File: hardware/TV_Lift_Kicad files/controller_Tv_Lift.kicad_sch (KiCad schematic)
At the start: 102 parts, among them J1 socket LAN8720a, J10 1844210, J11 1844223, J12 C5360899, J2 1836189, J3 1844223, J4 1844210, J5 1844223, J6 1844223, J7 1844236, J8 C5360899, J9 1844210, Q2 MMBT3906, SW1 TS-1187A-BAB, SW2 TS-1187A-BAB, SW3 TS-1187A-BAB, SW4 TS-1187A-BAB, U1 MAX3232, U10 VNH5019A-E, U2 TSOP32S40F, U3 SN65HVD230, U4 ESP32-WROOM-32, U5 LM2596S-5, U6 AMS1117-3.3, U7 PC817, U8 PC817, U9 b0505s-1we

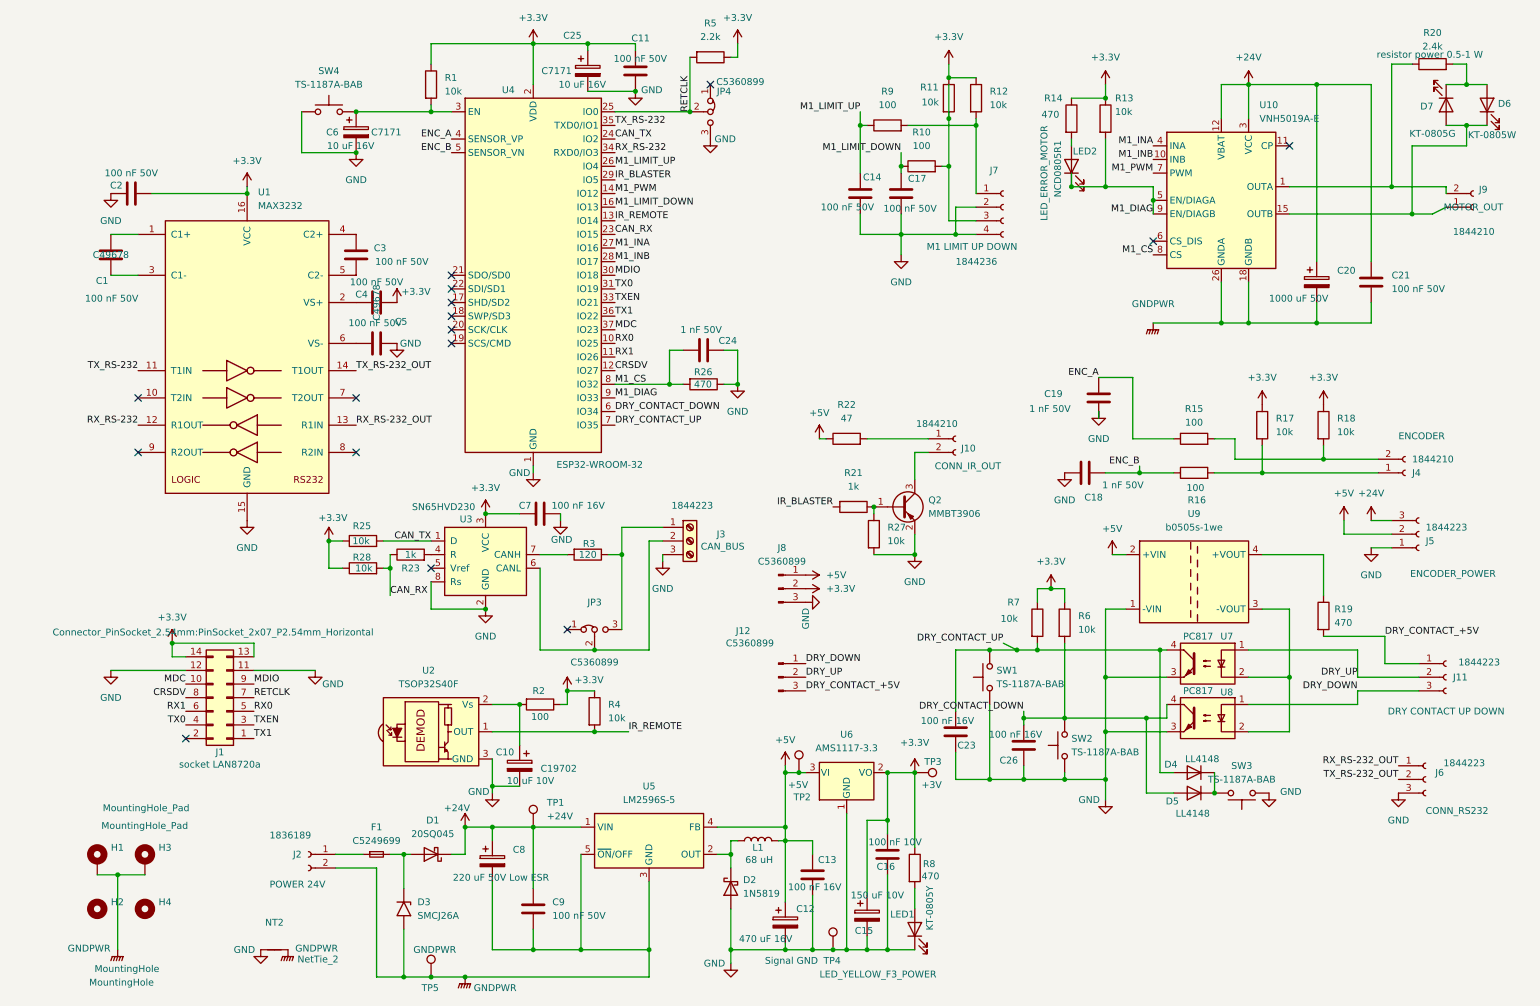
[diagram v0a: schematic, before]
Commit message: finish pcb board change pins
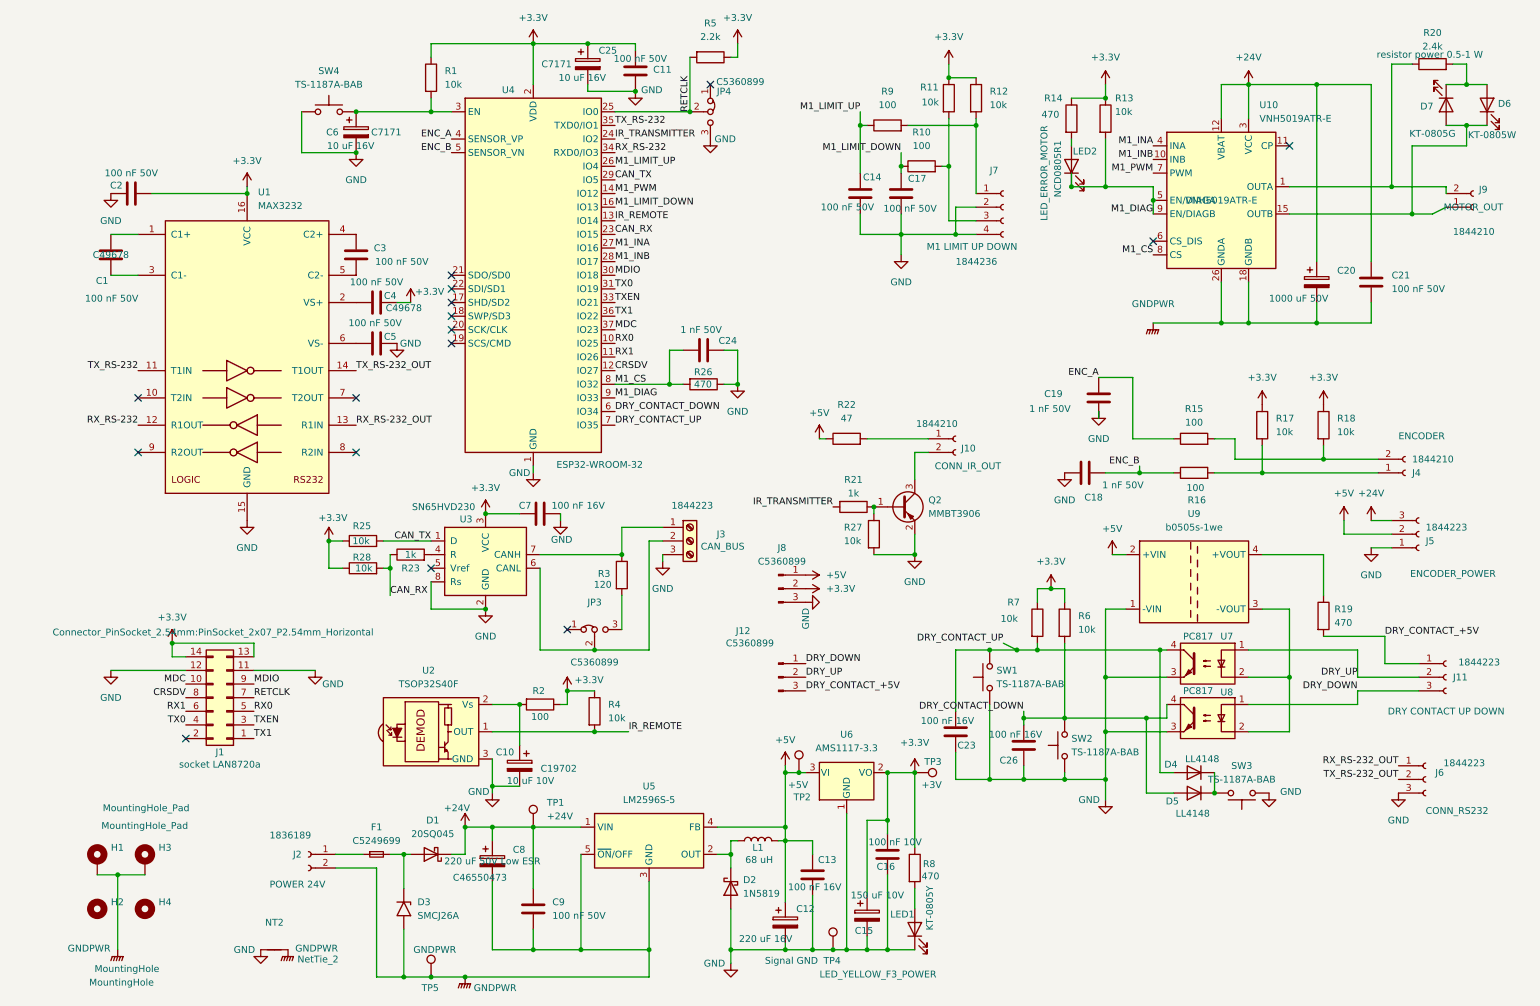
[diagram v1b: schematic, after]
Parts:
- C12: value 470 uF 16V -> 220 uF 16V
- C8: value 220 uF 50V Low ESR -> C46550473; footprint Capacitor_THT:CP_Radial_D6.3mm_P2.50mm -> Capacitor_SMD:CP_Elec_10x10
- TP1, TP2, TP3, TP4, TP5: now left out of the parts list
- U10: value VNH5019A-E -> VNH5019ATR-E
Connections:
- net CAN_TX: now also U4.29 (IO5); no longer U4.24 (IO2)
- net at J3.1 (Pin_1), R3.1: now also U3.7 (CANH); no longer JP3.3 (B)
- net at R3.2: now also JP3.3 (B); no longer U3.7 (CANH)
- net IR_BLASTER renamed IR_TRANSMITTER
- net IR_TRANSMITTER: now also U4.24 (IO2); no longer U4.29 (IO5)
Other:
- moved on the sheet: C25, R1, R3

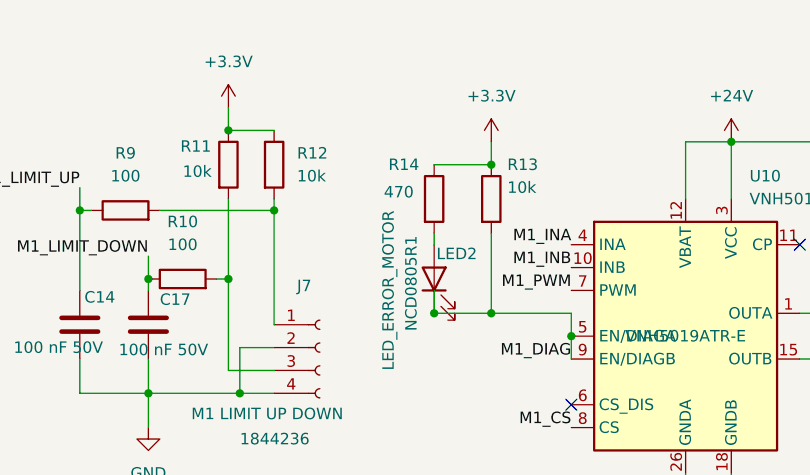
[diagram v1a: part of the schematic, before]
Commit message: add  option current sensor
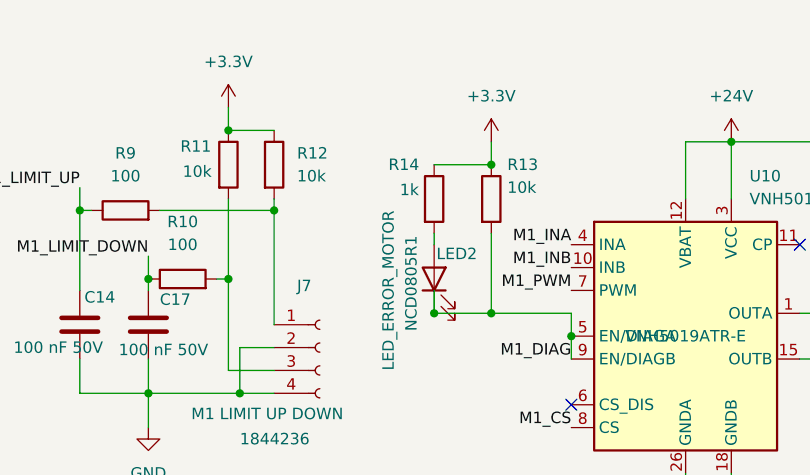
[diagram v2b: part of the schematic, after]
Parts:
- R14: value 470 -> 1k
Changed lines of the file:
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@@
 			)
 		)
-		(property "Value" "470"
-			(at 195.072 32.258 0)
+		(property "Value" "1k"
+			(at 196.85 32.004 0)
 			(show_name no)
 			(do_not_autoplace no)

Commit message: fix  overcurrent
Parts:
- R14: value 1k -> 470
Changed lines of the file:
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@@
 			)
 		)
-		(property "Value" "1k"
-			(at 196.85 32.004 0)
+		(property "Value" "470"
+			(at 195.072 32.258 0)
 			(show_name no)
 			(do_not_autoplace no)
